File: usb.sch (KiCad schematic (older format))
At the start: 25 parts, among them J4 CONN_02X03, U1 LFE5U-85F-6BG381C, U6 FT231XS, Y1 FNETHE025

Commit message: First pass cleanup
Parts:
- removed R56: 0, Resistor_SMD:R_0603_1608Metric, symbol Device:R
- removed R9: 15k, Resistor_SMD:R_0603_1608Metric, symbol Device:R
- removed U6: FT231XS, ft231x:FT231X-SSOP-20_4.4x6.5mm_Pitch0.65mm, symbol ftdi:FT231XS
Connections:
- net labels removed: FT2V5, FTDI_nSLEEP, FTDI_nTXLED, nRESET
- wire segments 74 -> 51
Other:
- note removed: "Short circuit R56\nfor chip rev A,B,C\nworkaround in \nTN140_FT231X Errata"
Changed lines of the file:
@@
 EESchema Schematic File Version 4
-EELAYER 30 0
+LIBS:ulx3s-cache
+EELAYER 29 0
 EELAYER END
 $Descr A4 11693 8268
@@
 	1    0    0    -1
 $EndComp
-$Comp
-L power:GND #PWR0111
-U 1 1 58D8877C
-P 5600 4500
-F 0 "#PWR0111" H 5600 4250 50  0001 C CNN
-F 1 "GND" H 5600 4350 50  0000 C CNN
-F 2 "" H 5600 4500 50  0000 C CNN
-F 3 "" H 5600 4500 50  0000 C CNN
-	1    5600 4500
-	1    0    0    -1
-$EndComp
-Text GLabel 5000 3100 0    60   Input ~ 0
-USB_FTDI_D-
-Text GLabel 5000 3200 0    60   Input ~ 0
-USB_FTDI_D+
-Text GLabel 6550 3300 2    60   Input ~ 0
-JTAG_TCK
-Text GLabel 6550 3500 2    60   Input ~ 0
-JTAG_TDI
-Text GLabel 6550 3100 2    60   Input ~ 0
-JTAG_TDO
-Text GLabel 6550 3400 2    60   Input ~ 0
-JTAG_TMS
-Text GLabel 6550 2800 2    60   Input ~ 0
-FTDI_TXD
-Text GLabel 6550 2900 2    60   Input ~ 0
-FTDI_RXD
-Text GLabel 6550 3000 2    60   Input ~ 0
-FTDI_nRTS
-Text GLabel 6550 3200 2    60   Input ~ 0
-FTDI_nDTR
 Text GLabel 9300 3800 2    60   Input ~ 0
 JTAG_TDI
@@
 Text GLabel 2150 1500 2    60   Input ~ 0
 USB5V
-$Comp
-L ftdi:FT231XS U6
-U 1 1 58EB61C6
-P 5700 3400
-F 0 "U6" H 5150 4200 50  0000 L CNN
-F 1 "FT231XS" H 6000 4200 50  0000 L CNN
-F 2 "ft231x:FT231X-SSOP-20_4.4x6.5mm_Pitch0.65mm" H 5700 3400 50  0001 C CNN
-F 3 "www.ftdichip.com/Documents/DataSheets/ICs/DS_FT231X.pdf" H 5700 3400 50  0001 C CNN
-F 4 "www.ftdichip.com" H 5700 3400 60  0001 C CNN "MNF1_URL"
-F 5 "FT231XS" H 5700 3400 60  0001 C CNN "MPN"
-F 6 "895-FT231XS-R" H 5700 3400 60  0001 C CNN "Mouser"
-F 7 "768-1129-1-ND" H 5700 3400 50  0001 C CNN "Digikey"
-F 8 "C132160" H 5700 3400 50  0001 C CNN "LCSC"
-F 9 "7570032" H 5700 3400 50  0001 C CNN "RS"
-F 10 "1.86$" H 5700 3400 50  0001 C CNN "price100_RS"
-F 11 "FU002" H 5700 3400 50  0001 C CNN "Koncar"
-	1    5700 3400
-	1    0    0    -1
-$EndComp
 Wire Wire Line
 	1800 1700 1950 1700
@@
 Wire Wire Line
 	1800 2000 1850 2000
-Wire Wire Line
-	5600 4300 5600 4400
-Connection ~ 5600 4400
-Wire Wire Line
-	6400 3700 6450 3700
-Wire Wire Line
-	6400 3800 6550 3800
-Wire Wire Line
-	6400 3900 6550 3900
-Wire Wire Line
-	6400 4000 6550 4000
-Wire Wire Line
-	6400 2800 6550 2800
-Wire Wire Line
-	6400 2900 6550 2900
-Wire Wire Line
-	6400 3000 6550 3000
-Wire Wire Line
-	6400 3100 6550 3100
-Wire Wire Line
-	6400 3200 6550 3200
-Wire Wire Line
-	6400 3300 6550 3300
-Wire Wire Line
-	6400 3400 6550 3400
-Wire Wire Line
-	6400 3500 6550 3500
 Wire Wire Line
 	2150 1500 1950 1500
@@
 	1950 1500 1950 1700
 Connection ~ 1950 1700
-Wire Wire Line
-	5600 4400 5800 4400
-Wire Wire Line
-	5800 4400 5800 4300
-Text GLabel 4850 3400 0    60   Input ~ 0
-nRESET
-Wire Wire Line
-	4850 3400 4950 3400
-$Comp
-L Device:R R9
-U 1 1 58EB9CB5
-P 4700 3600
-AR Path="/58EB9CB5" Ref="R9"  Part="1"
-AR Path="/58D6BF46/58EB9CB5" Ref="R9"  Part="1"
-F 0 "R9" V 4780 3600 50  0000 C CNN
-F 1 "15k" V 4700 3600 50  0000 C CNN
-F 2 "Resistor_SMD:R_0603_1608Metric" V 4630 3600 50  0001 C CNN
-F 3 "" H 4700 3600 50  0000 C CNN
-F 4 "www.yageo.com" V 4700 3600 50  0001 C CNN "MNF1_URL"
-F 5 "RC0603FR-0715KL" V 4700 3600 50  0001 C CNN "MPN"
-F 6 "603-RC0603FR-0715KL" V 4700 3600 50  0001 C CNN "Mouser"
-F 7 "603-RC0603FR-1015KL" V 4700 3600 50  0001 C CNN "Mouse_r2"
-F 8 "603-RC0603FR-1315KL" V 4700 3600 50  0001 C CNN "Mouse_r3"
-F 9 "YAG3569CT-ND" V 4700 3600 50  0001 C CNN "Digikey"
-F 10 "C217750" V 4700 3600 50  0001 C CNN "LCSC"
-F 11 "8.4$" V 4700 3600 50  0001 C CNN "price1500_Mouser"
-F 12 "FR005" V 4700 3600 50  0001 C CNN "Koncar"
-	1    4700 3600
-	0    1    1    0
-$EndComp
-Wire Wire Line
-	4850 3600 4950 3600
-Wire Wire Line
-	4950 3600 4950 3400
-Connection ~ 4950 3400
-Wire Wire Line
-	4550 3600 4450 3600
 Text GLabel 10150 2650 2    60   Input ~ 0
 FTDI_TXD
@@
 Text Notes 7400 3650 0    60   ~ 0
 FTDI default
-Text GLabel 6550 4000 2    60   Input ~ 0
-FTDI_nSLEEP
-Text GLabel 6550 3700 2    60   Input ~ 0
-FTDI_TXDEN
-Text GLabel 6550 3800 2    60   Input ~ 0
-FTDI_nRXLED
-Text GLabel 6550 3900 2    60   Input ~ 0
-FTDI_nTXLED
 Text Notes 7200 3450 0    60   ~ 0
 VNC2 programming pins:\nTXD RXD TXDEN
@@
 Text GLabel 8650 2350 0    60   Input ~ 0
 FTDI_TXDEN
-$Comp
-L Device:R R56
-U 1 1 59DFFFBE
-P 6450 4250
-AR Path="/59DFFFBE" Ref="R56"  Part="1"
-AR Path="/58D6BF46/59DFFFBE" Ref="R56"  Part="1"
-F 0 "R56" V 6530 4250 50  0000 C CNN
-F 1 "0" V 6450 4250 50  0000 C CNN
-F 2 "Resistor_SMD:R_0603_1608Metric" V 6380 4250 50  0001 C CNN
-F 3 "" H 6450 4250 50  0000 C CNN
-F 4 "Leave empty" H 6450 4250 60  0001 C CNN "Note"
-F 5 "www.yageo.com" V 6450 4250 50  0001 C CNN "MNF1_URL"
-F 6 "RC0603JR-070RL" V 6450 4250 50  0001 C CNN "EMPTY_MPN"
-	1    6450 4250
-	-1   0    0    1
-$EndComp
-Wire Wire Line
-	6450 4100 6450 3700
-Connection ~ 6450 3700
-$Comp
-L power:GND #PWR0112
-U 1 1 59E000AB
-P 6450 4400
-F 0 "#PWR0112" H 6450 4150 50  0001 C CNN
-F 1 "GND" H 6450 4250 50  0000 C CNN
-F 2 "" H 6450 4400 50  0000 C CNN
-F 3 "" H 6450 4400 50  0000 C CNN
-	1    6450 4400
-	1    0    0    -1
-$EndComp
-Text Notes 6100 5000 0    60   ~ 0
-Short circuit R56\nfor chip rev A,B,C\nworkaround in \nTN140_FT231X Errata
 $Comp
 L lfe5bg381:LFE5UM-85F-6BG381C U1
@@
 	1    0    0    -1
 $EndComp
-Text GLabel 4450 3600 0    60   Input ~ 0
-FT2V5
-Text GLabel 5800 2500 1    60   Input ~ 0
-FT2V5
-Text GLabel 5000 2800 0    60   Input ~ 0
-FT2V5
-Text GLabel 5600 2500 1    60   Input ~ 0
-USB5V
 Text Notes 6300 2500 0    60   ~ 0
 WIFI_GPIO15 v1.7 WIFI_GPIO17 <v3.1
@@
 D+,D- 15k pulldown \nfor host mode
 Wire Wire Line
-	5600 4400 5600 4500
-Wire Wire Line
 	1950 1700 2200 1700
 Wire Wire Line
-	4950 3400 5000 3400
-Wire Wire Line
 	2650 3200 2700 3200
 Wire Wire Line
@@
 	2700 2750 3000 2750
 Wire Wire Line
-	6450 3700 6550 3700
-Wire Wire Line
 	5450 1200 5450 1250

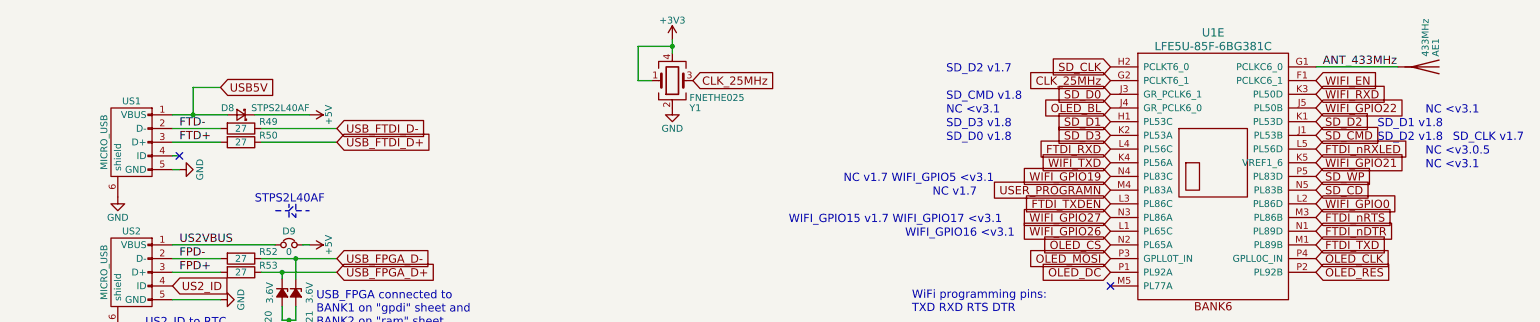
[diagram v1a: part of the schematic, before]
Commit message: More cleanup - moving flash and crystal
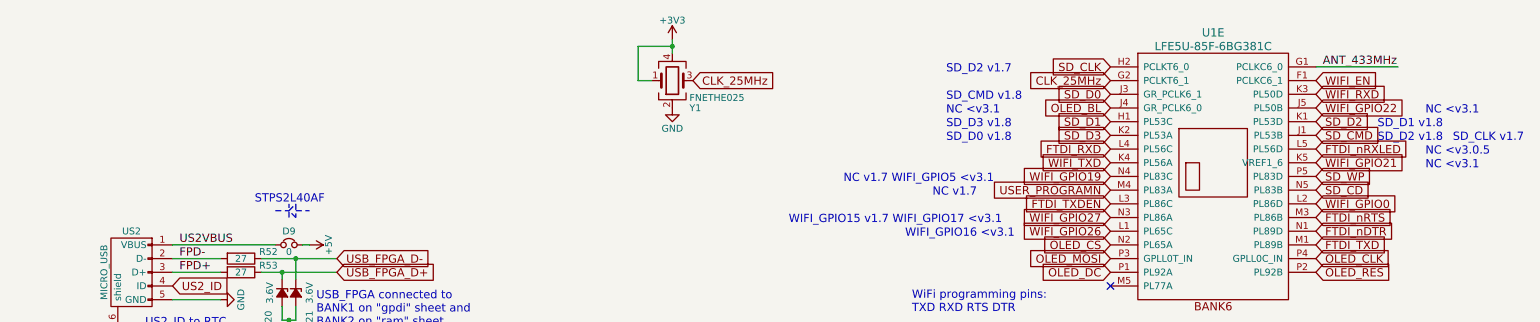
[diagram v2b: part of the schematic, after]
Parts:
- removed AE1: 433MHz, TestPoint:TestPoint_Pad_D1.0mm, symbol Device:Antenna
- removed D8: STPS2L40AF, Diode_SMD:D_SMA, symbol Device:D_Schottky_Small
- removed R49, R50: 27, Resistor_SMD:R_0603_1608Metric, symbol Device:R
- removed US1: MICRO_USB, usb_otg:USB-MICRO-B-FCI-10118192-0001LF, symbol usb_otg:USB_OTG
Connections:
- no-connect marks 2 -> 1
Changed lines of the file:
@@
 $EndDescr
-$Comp
-L Device:D_Schottky_Small D8
-U 1 1 58D6C83A
-P 2300 1700
-F 0 "D8" H 2350 1650 50  0000 L CNN
-F 1 "STPS2L40AF" H 1800 1650 50  0000 L CNN
-F 2 "Diode_SMD:D_SMA" V 2300 1700 60  0001 C CNN
-F 3 "" V 2300 1700 60  0000 C CNN
-F 4 "www.st.com" H 2300 1700 50  0001 C CNN "MNF1_URL"
-F 5 "STPS2L30AF" H 2300 1700 60  0001 C CNN "MPN"
-F 6 "511-STPS2L40AF" H 2300 1700 60  0001 C CNN "Mouser"
-F 7 "497-12310-1-ND" H 2300 1700 50  0001 C CNN "Digikey"
-F 8 "STPS2L30AF" H 2300 1700 50  0001 C CNN "AvnetEU"
-F 9 "C111630" H 2300 1700 50  0001 C CNN "LCSC"
-F 10 "0.22121$" H 2300 1700 50  0001 C CNN "price100_AvnetEU"
-F 11 "FV008" H 2300 1700 50  0001 C CNN "Koncar"
-	1    2300 1700
-	-1   0    0    1
-$EndComp
-$Comp
-L power:+5V #PWR0107
-U 1 1 58D6C83B
-P 2800 1700
-F 0 "#PWR0107" H 2800 1550 50  0001 C CNN
-F 1 "+5V" H 2800 1840 50  0000 C CNN
-F 2 "" H 2800 1700 60  0000 C CNN
-F 3 "" H 2800 1700 60  0000 C CNN
-	1    2800 1700
-	0    1    1    0
-$EndComp
 $Comp
 L Device:Jumper_NC_Small D9
@@
 $EndComp
 $Comp
-L usb_otg:USB_OTG US1
-U 1 1 58D6C840
-P 1500 1900
-AR Path="/58D6C840" Ref="US1"  Part="1"
-AR Path="/58D6BF46/58D6C840" Ref="US1"  Part="1"
-F 0 "US1" V 1200 1900 50  0000 C CNN
-F 1 "MICRO_USB" H 1500 2100 50  0000 C CNN
-F 2 "usb_otg:USB-MICRO-B-FCI-10118192-0001LF" V 1450 1800 50  0001 C CNN
-F 3 "http://portal.fciconnect.com/Comergent/fci/drawing/10118192.pdf" H 1450 1800 50  0001 C CNN
-F 4 "FCI" H 1500 1900 50  0001 C CNN "MFG1"
-F 5 "www.fciconnect.com" H 1500 1900 60  0001 C CNN "MNF1_URL"
-F 6 "10118192-0001LF" H 1500 1900 60  0001 C CNN "MPN"
-F 7 "https://www.molex.com/pdm_docs/sd/473460001_sd.pdf" H 1500 1900 50  0001 C CNN "Datasheet2"
-F 8 "Molex" H 1500 1900 50  0001 C CNN "MFG2"
-F 9 "www.molex.com" H 1500 1900 50  0001 C CNN "MNF2_URL"
-F 10 "47346-0001" H 1500 1900 50  0001 C CNN "MPN2"
-F 11 "538-47346-0001" H 1500 1900 50  0001 C CNN "Mouser"
-F 12 "649-10118192-0001LF " H 1500 1900 50  0001 C CNN "Mouse_r1"
-F 13 "609-4613-1-ND" H 1500 1900 50  0001 C CNN "Digikey"
-F 14 "WM17141CT-ND" H 1500 1900 50  0001 C CNN "Digikey2"
-F 15 "C132564" V 1500 1900 50  0001 C CNN "LCSC"
-F 16 "10118192-0001LF" V 1500 1900 50  0001 C CNN "FreelanceElec"
-F 17 "0.12487$" V 1500 1900 50  0001 C CNN "price200_FreelanceElec"
-F 18 "FU010" V 1500 1900 50  0001 C CNN "Koncar"
-F 19 "T" V 1500 1900 50  0001 C CNN "Side"
-	1    1500 1900
-	0    -1   1    0
-$EndComp
-$Comp
 L usb_otg:USB_OTG US2
 U 1 1 58D6C841
@@
 $EndComp
 $Comp
-L power:GND #PWR0104
-U 1 1 58D6C842
-P 1850 2100
-F 0 "#PWR0104" H 1850 1850 50  0001 C CNN
-F 1 "GND" H 1850 1950 50  0000 C CNN
-F 2 "" H 1850 2100 50  0000 C CNN
-F 3 "" H 1850 2100 50  0000 C CNN
-	1    1850 2100
-	0    -1   -1   0
-$EndComp
-$Comp
 L power:GND #PWR0105
 U 1 1 58D6C843
@@
 	0    -1   -1   0
 $EndComp
-Text GLabel 3000 1800 2    60   Input ~ 0
-USB_FTDI_D-
-Text GLabel 3000 1900 2    60   Input ~ 0
-USB_FTDI_D+
 Text GLabel 3000 2750 2    60   Input ~ 0
 USB_FPGA_D-
 Text GLabel 3000 2850 2    60   Input ~ 0
 USB_FPGA_D+
-NoConn ~ 1850 2000
-$Comp
-L power:GND #PWR0102
-U 1 1 58D82518
-P 1400 2300
-F 0 "#PWR0102" H 1400 2050 50  0001 C CNN
-F 1 "GND" H 1400 2150 50  0000 C CNN
-F 2 "" H 1400 2300 50  0000 C CNN
-F 3 "" H 1400 2300 50  0000 C CNN
-	1    1400 2300
-	1    0    0    -1
-$EndComp
 $Comp
 L power:GND #PWR0103
@@
 Text GLabel 9300 4100 2    60   Input ~ 0
 JTAG_TMS
-Text GLabel 2150 1500 2    60   Input ~ 0
-USB5V
-Wire Wire Line
-	1800 1700 1950 1700
-Wire Wire Line
-	2400 1700 2800 1700
 Wire Wire Line
 	2750 2650 2800 2650
@@
 	1800 2650 2550 2650
 Wire Wire Line
-	1800 2100 1850 2100
-Wire Wire Line
 	1800 3050 2150 3050
 Wire Wire Line
-	1800 1800 2150 1800
-Wire Wire Line
-	1800 1900 2150 1900
-Wire Wire Line
 	1800 2750 2150 2750
 Wire Wire Line
 	1800 2850 2150 2850
-Wire Wire Line
-	1800 2000 1850 2000
-Wire Wire Line
-	2150 1500 1950 1500
-Wire Wire Line
-	1950 1500 1950 1700
-Connection ~ 1950 1700
 Text GLabel 10150 2650 2    60   Input ~ 0
 FTDI_TXD
@@
 Wire Wire Line
 	8700 4900 9150 4900
-$Comp
-L Device:R R49
-U 1 1 59274246
-P 2300 1800
-AR Path="/59274246" Ref="R49"  Part="1"
-AR Path="/58D6BF46/59274246" Ref="R49"  Part="1"
-F 0 "R49" V 2250 2000 50  0000 C CNN
-F 1 "27" V 2300 1800 50  0000 C CNN
-F 2 "Resistor_SMD:R_0603_1608Metric" V 2230 1800 50  0001 C CNN
-F 3 "" H 2300 1800 50  0000 C CNN
-F 4 "www.yageo.com" V 2300 1800 50  0001 C CNN "MNF1_URL"
-F 5 "AC0603JR-0727RL" V 2300 1800 50  0001 C CNN "MPN"
-F 6 "603-AC0603JR-0727RL" V 2300 1800 50  0001 C CNN "Mouser"
-F 7 "311-27.0HRCT-ND" V 2300 1800 50  0001 C CNN "Digikey"
-F 8 "C325726" V 2300 1800 50  0001 C CNN "LCSC"
-F 9 "FR008" V 2300 1800 50  0001 C CNN "Koncar"
-	1    2300 1800
-	0    1    1    0
-$EndComp
-$Comp
-L Device:R R50
-U 1 1 592743C8
-P 2300 1900
-AR Path="/592743C8" Ref="R50"  Part="1"
-AR Path="/58D6BF46/592743C8" Ref="R50"  Part="1"
-F 0 "R50" V 2250 2100 50  0000 C CNN
-F 1 "27" V 2300 1900 50  0000 C CNN
-F 2 "Resistor_SMD:R_0603_1608Metric" V 2230 1900 50  0001 C CNN
-F 3 "" H 2300 1900 50  0000 C CNN
-F 4 "www.yageo.com" V 2300 1900 50  0001 C CNN "MNF1_URL"
-F 5 "AC0603JR-0727RL" V 2300 1900 50  0001 C CNN "MPN"
-	1    2300 1900
-	0    1    1    0
-$EndComp
-Wire Wire Line
-	2450 1800 3000 1800
-Wire Wire Line
-	2450 1900 3000 1900
-Text Label 1850 1800 0    60   ~ 0
-FTD-
-Text Label 1850 1900 0    60   ~ 0
-FTD+
 Text Notes 2850 3250 0    60   ~ 0
 USB_FPGA connected to\nBANK1 on "gpdi" sheet and\nBANK2 on "ram" sheet
@@
 Text GLabel 8650 2550 0    60   Input ~ 0
 WIFI_GPIO26
-$Comp
-L Device:Antenna AE1
-U 1 1 59C3AE47
-P 10950 1350
-AR Path="/59C3AE47" Ref="AE1"  Part="1"
-AR Path="/58D6BF46/59C3AE47" Ref="AE1"  Part="1"
-F 0 "AE1" H 10875 1425 50  0000 R CNN
-F 1 "433MHz" H 10875 1350 50  0000 R CNN
-F 2 "TestPoint:TestPoint_Pad_D1.0mm" H 10950 1350 50  0001 C CNN
-F 3 "" H 10950 1350 50  0001 C CNN
-F 4 "Leave empty" H 10950 1350 60  0001 C CNN "Note"
-	1    10950 1350
-	0    1    1    0
-$EndComp
 Wire Wire Line
 	10150 1350 10750 1350
@@
 D+,D- 15k pulldown \nfor host mode
 Wire Wire Line
-	1950 1700 2200 1700
-Wire Wire Line
 	2650 3200 2700 3200
